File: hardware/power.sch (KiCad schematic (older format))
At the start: 79 parts, among them CON1 BARREL_JACK, U26 TPS5420D, U27 TPS5420D, U28 TPS560200, U29 LP2985A-10DBVR, U30 TPS7A7001DDA, U31 TPS7A91, U32 TPS7A91, U33 LP5907MFX-3.0, U34 TPS7A91

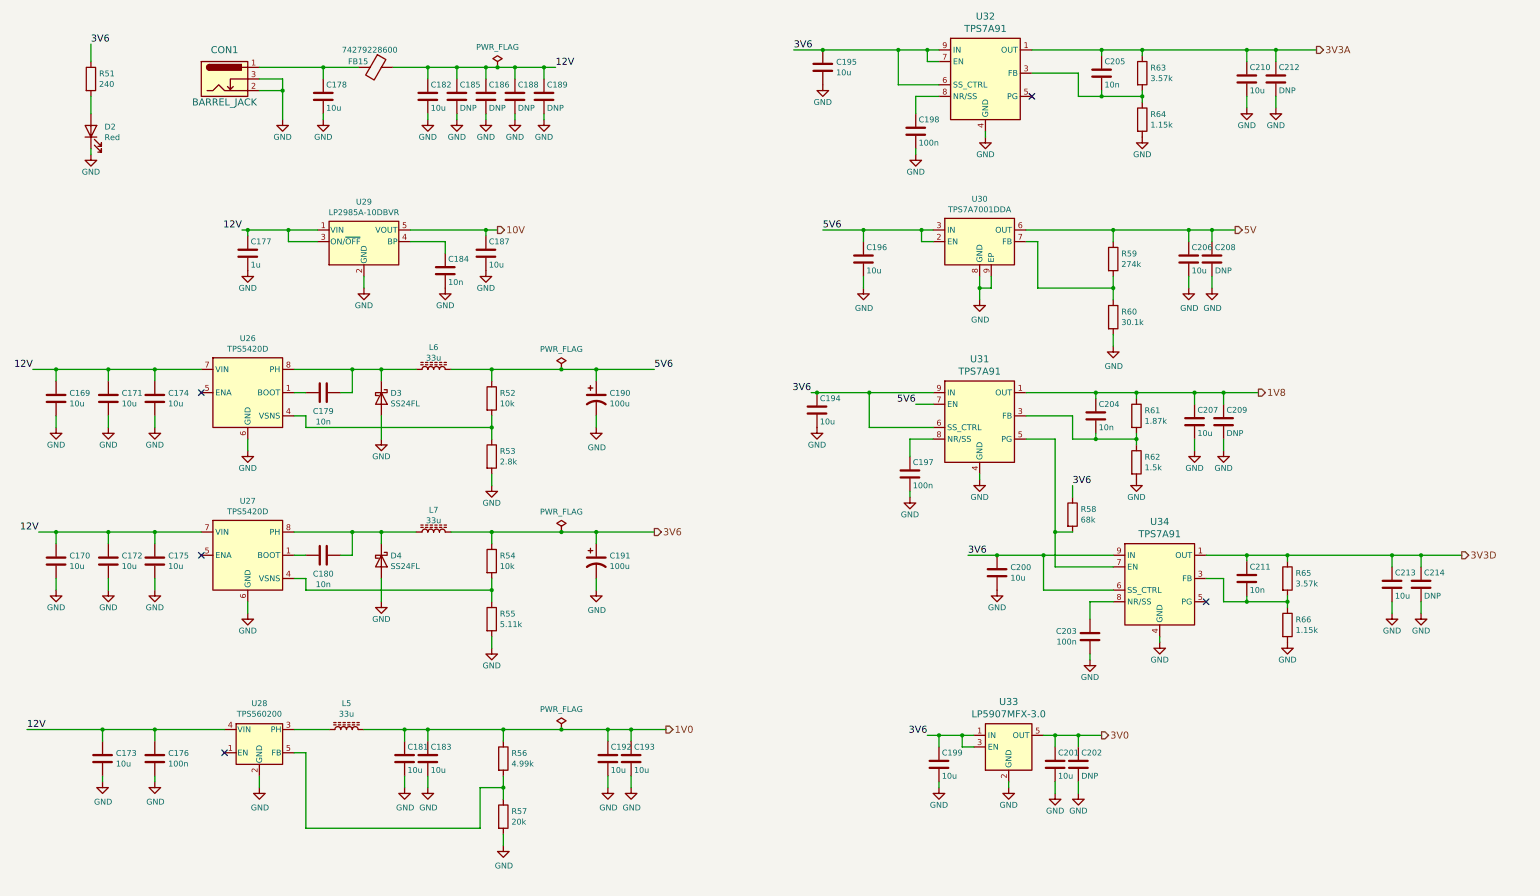
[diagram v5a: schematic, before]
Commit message: Completed clock placement and routing.
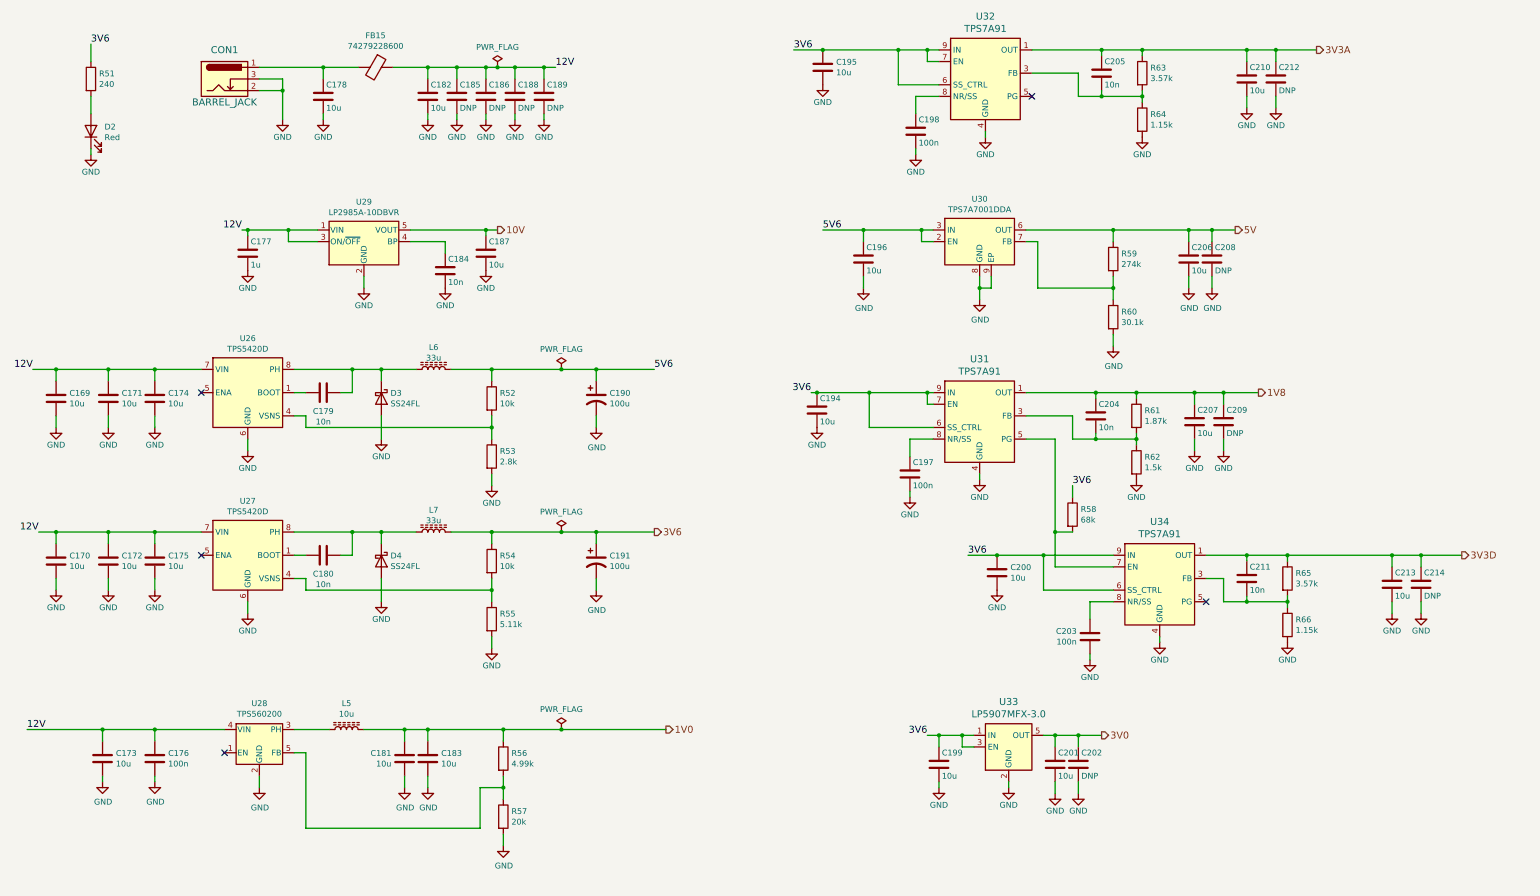
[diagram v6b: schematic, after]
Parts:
- removed C192, C193: 10u, Capacitor_SMD:C_0805_2012Metric, symbol Device:C
- L5: value 33u -> 10u; footprint Inductor_SMD:L_Bourns_SRR1210A -> Inductor_SMD:L_Wuerth_WE-PD-Typ-7345; MFN SRR1210A-330M -> 744777910
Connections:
- net 3V6: now also U31.7 (EN)
- net 5V6: no longer U31.7 (EN)
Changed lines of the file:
@@
 U 1 1 593D9669
 P 5200 2150
-F 0 "FB15" V 5150 2000 50  0000 C CNN
-F 1 "74279228600" V 5050 2100 50  0000 C CNN
+F 0 "FB15" V 4926 2150 50  0000 C CNN
+F 1 "74279228600" V 5017 2150 50  0000 C CNN
 F 2 "Inductor_SMD:L_0603_1608Metric" H 5200 2150 60  0001 C CNN
 F 3 "https://katalog.we-online.de/pbs/datasheet/74279228600.pdf" H 5200 2150 60  0001 C CNN
@@
 	1    0    0    -1
 $EndComp
-Text Label 9850 5050 2    60   ~ 0
-5V6
 $Comp
 L Device:C C202
@@
 	8950 4950 9000 4950
 Wire Wire Line
-	9850 5050 10000 5050
+	9950 5050 10000 5050
 Connection ~ 9000 4950
 Connection ~ 12500 4950
@@
 	1    0    0    -1
 $EndComp
-$Comp
-L power:GND #PWR0197
-U 1 1 5C36EE88
-P 5650 8350
-F 0 "#PWR0197" H 5650 8100 50  0001 C CNN
-F 1 "GND" H 5655 8177 50  0000 C CNN
-F 2 "" H 5650 8350 50  0001 C CNN
-F 3 "" H 5650 8350 50  0001 C CNN
-	1    5650 8350
-	1    0    0    -1
-$EndComp
-Wire Wire Line
-	5650 8350 5650 8250
 Wire Wire Line
 	5450 8250 5450 8350
@@
 	5450 7950 5450 7850
 Connection ~ 5450 7850
-Wire Wire Line
-	5450 7850 5650 7850
-Wire Wire Line
-	5650 7850 5650 7950
-Connection ~ 5650 7850
-Wire Wire Line
-	5650 7850 6300 7850
 $Comp
 L power:GND #PWR0204
@@
 Wire Wire Line
 	6300 7850 6800 7850
-$Comp
-L power:GND #PWR0209
-U 1 1 5C484E9F
-P 7200 8350
-F 0 "#PWR0209" H 7200 8100 50  0001 C CNN
-F 1 "GND" H 7205 8177 50  0000 C CNN
-F 2 "" H 7200 8350 50  0001 C CNN
-F 3 "" H 7200 8350 50  0001 C CNN
-	1    7200 8350
-	1    0    0    -1
-$EndComp
-$Comp
-L power:GND #PWR0210
-U 1 1 5C484EA5
-P 7400 8350
-F 0 "#PWR0210" H 7400 8100 50  0001 C CNN
-F 1 "GND" H 7405 8177 50  0000 C CNN
-F 2 "" H 7400 8350 50  0001 C CNN
-F 3 "" H 7400 8350 50  0001 C CNN
-	1    7400 8350
-	1    0    0    -1
-$EndComp
-Wire Wire Line
-	7400 8350 7400 8250
-Wire Wire Line
-	7200 8250 7200 8350
-Wire Wire Line
-	7200 7950 7200 7850
-Connection ~ 7200 7850
-Wire Wire Line
-	7200 7850 7400 7850
-Wire Wire Line
-	7400 7850 7400 7950
-Connection ~ 7400 7850
-Wire Wire Line
-	7400 7850 7700 7850
 $Comp
 L Device:C C173
@@
 U 1 1 5C4FE515
 P 5450 8100
-F 0 "C181" H 5475 8200 50  0000 L CNN
-F 1 "10u" H 5475 8000 50  0000 L CNN
+F 0 "C181" H 5336 8146 50  0000 R CNN
+F 1 "10u" H 5336 8055 50  0000 R CNN
 F 2 "Capacitor_SMD:C_0805_2012Metric" H 5488 7950 30  0001 C CNN
 F 3 "" H 5450 8100 60  0000 C CNN
@@
 	1    0    0    -1
 $EndComp
-$Comp
-L Device:C C183
-U 1 1 5C4FE5C3
-P 5650 8100
-F 0 "C183" H 5675 8200 50  0000 L CNN
-F 1 "10u" H 5675 8000 50  0000 L CNN
-F 2 "Capacitor_SMD:C_0805_2012Metric" H 5688 7950 30  0001 C CNN
-F 3 "" H 5650 8100 60  0000 C CNN
-F 4 "CL21B106KQQNNNE" H 2800 300 50  0001 C CNN "MFN"
-	1    5650 8100
-	1    0    0    -1
-$EndComp
-$Comp
-L Device:C C192
-U 1 1 5C4FE66D
-P 7200 8100
-F 0 "C192" H 7225 8200 50  0000 L CNN
-F 1 "10u" H 7225 8000 50  0000 L CNN
-F 2 "Capacitor_SMD:C_0805_2012Metric" H 7238 7950 30  0001 C CNN
-F 3 "" H 7200 8100 60  0000 C CNN
-F 4 "CL21B106KQQNNNE" H 4350 300 50  0001 C CNN "MFN"
-	1    7200 8100
-	1    0    0    -1
-$EndComp
-$Comp
-L Device:C C193
-U 1 1 5C4FE719
-P 7400 8100
-F 0 "C193" H 7425 8200 50  0000 L CNN
-F 1 "10u" H 7425 8000 50  0000 L CNN
-F 2 "Capacitor_SMD:C_0805_2012Metric" H 7438 7950 30  0001 C CNN
-F 3 "" H 7400 8100 60  0000 C CNN
-F 4 "CL21B106KQQNNNE" H 4550 300 50  0001 C CNN "MFN"
-	1    7400 8100
-	1    0    0    -1
-$EndComp
 NoConn ~ 3900 8050
 $Comp
@@
 P 4950 7850
 F 0 "L5" V 5175 7850 50  0000 C CNN
-F 1 "33u" V 5084 7850 50  0000 C CNN
-F 2 "Inductor_SMD:L_Bourns_SRR1210A" H 4950 7850 50  0001 C CNN
+F 1 "10u" V 5084 7850 50  0000 C CNN
+F 2 "Inductor_SMD:L_Wuerth_WE-PD-Typ-7345" H 4950 7850 50  0001 C CNN
 F 3 "~" H 4950 7850 50  0001 C CNN
-F 4 "SRR1210A-330M" H 4950 7850 50  0001 C CNN "MFN"
+F 4 "744777910" H 4950 7850 50  0001 C CNN "MFN"
 	1    4950 7850
 	0    -1   -1   0
@@
 $EndComp
 Connection ~ 6800 7850
-Wire Wire Line
-	6800 7850 7200 7850
 $Comp
 L power:PWR_FLAG #FLG017
@@
 	6250 2150 6400 2150
 Wire Wire Line
-	6300 8250 6300 8350
-Wire Wire Line
-	6300 8350 6100 8350
-Wire Wire Line
-	6100 8350 6100 8700
-Wire Wire Line
-	6100 8700 4600 8700
-Wire Wire Line
 	4600 8700 4600 8050
-Connection ~ 6300 8350
-Wire Wire Line
-	6300 8350 6300 8450
 Wire Wire Line
 	10800 5350 11050 5350
@@
 	10800 5150 11200 5150
 Wire Wire Line
-	9450 4950 10000 4950
+	9450 4950 9950 4950
 Wire Wire Line
 	9450 5250 10000 5250
@@
 	10850 2000 11450 2000
 NoConn ~ 10850 2400
+Wire Wire Line
+	6800 7850 7700 7850
+Connection ~ 6300 8350
+Wire Wire Line
+	6300 8350 6300 8450
+Wire Wire Line
+	6300 8250 6300 8350
+Wire Wire Line
+	6100 8700 4600 8700
+Wire Wire Line
+	5450 7850 5650 7850
+Wire Wire Line
+	6100 8350 6100 8700
+Wire Wire Line
+	6300 8350 6100 8350
+$Comp
+L Device:C C183
+U 1 1 5C4FE5C3
+P 5650 8100
+F 0 "C183" H 5765 8146 50  0000 L CNN
+F 1 "10u" H 5765 8055 50  0000 L CNN
+F 2 "Capacitor_SMD:C_0805_2012Metric" H 5688 7950 30  0001 C CNN
+F 3 "" H 5650 8100 60  0000 C CNN
+F 4 "CL21B106KQQNNNE" H 2800 300 50  0001 C CNN "MFN"
+	1    5650 8100
+	1    0    0    -1
+$EndComp
+Wire Wire Line
+	5650 7850 5650 7950
+Wire Wire Line
+	5650 8350 5650 8250
+$Comp
+L power:GND #PWR0197
+U 1 1 5C36EE88
+P 5650 8350
+F 0 "#PWR0197" H 5650 8100 50  0001 C CNN
+F 1 "GND" H 5655 8177 50  0000 C CNN
+F 2 "" H 5650 8350 50  0001 C CNN
+F 3 "" H 5650 8350 50  0001 C CNN
+	1    5650 8350
+	1    0    0    -1
+$EndComp
+Connection ~ 5650 7850
+Wire Wire Line
+	5650 7850 6300 7850
+Wire Wire Line
+	9950 5050 9950 4950
+Connection ~ 9950 4950
+Wire Wire Line
+	9950 4950 10000 4950
 $EndSCHEMATC

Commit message: Replaced relevant footprints for thermal via variety.
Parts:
- U30: footprint Package_SO:TI_SO-PowerPAD-8 -> Package_SO:TI_SO-PowerPAD-8_ThermalVias
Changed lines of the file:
@@
 F 0 "U30" H 10400 4017 50  0000 C CNN
 F 1 "TPS7A7001DDA" H 10400 3926 50  0000 C CNN
-F 2 "Package_SO:TI_SO-PowerPAD-8" H 10350 4000 50  0001 C CNN
+F 2 "Package_SO:TI_SO-PowerPAD-8_ThermalVias" H 10350 4000 50  0001 C CNN
 F 3 "www.ti.com/lit/ds/symlink/tps7a7001.pdf" H 10400 3650 50  0001 C CNN
 F 4 "TPS7A7001DDAR" H 0   0   50  0001 C CNN "MFN"
